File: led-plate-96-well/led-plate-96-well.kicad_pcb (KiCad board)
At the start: 2 copper layers, 175 x 100 mm, 2 parts, among them U1 TLC5947RHB, U2 A000053

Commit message: start main board
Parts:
- added C1: 100nF, Capacitor_SMD:C_0603_1608Metric, F.Cu at (100.2, 55.5)
- added C2: 10uF, Capacitor_SMD:C_0805_2012Metric, F.Cu at (92.2, 46.5)
- added D1: LED, SMD2835_WITH_STEP:LED_PLCC_2835, F.Cu at (99.1, 67.0)
- added D10: LED, SMD2835_WITH_STEP:LED_PLCC_2835, F.Cu at (112.4, 77.0)
- added D11: LED, SMD2835_WITH_STEP:LED_PLCC_2835, F.Cu at (112.4, 87.0)
- added D12: LED, SMD2835_WITH_STEP:LED_PLCC_2835, F.Cu at (112.4, 97.0)
- added D13: LED, SMD2835_WITH_STEP:LED_PLCC_2835, F.Cu at (112.4, 107.0)
- added D14: LED, SMD2835_WITH_STEP:LED_PLCC_2835, F.Cu at (112.4, 117.0)
- added D15: LED, SMD2835_WITH_STEP:LED_PLCC_2835, F.Cu at (112.4, 127.0)
- added D16: LED, SMD2835_WITH_STEP:LED_PLCC_2835, F.Cu at (112.4, 137.0)
- added D17: LED, SMD2835_WITH_STEP:LED_PLCC_2835, F.Cu at (124.1, 67.0)
- added D18: LED, SMD2835_WITH_STEP:LED_PLCC_2835, F.Cu at (124.1, 77.0)
- added D19: LED, SMD2835_WITH_STEP:LED_PLCC_2835, F.Cu at (124.1, 87.0)
- added D2: LED, SMD2835_WITH_STEP:LED_PLCC_2835, F.Cu at (99.1, 77.0)
- added D20: LED, SMD2835_WITH_STEP:LED_PLCC_2835, F.Cu at (124.1, 97.0)
- added D21: LED, SMD2835_WITH_STEP:LED_PLCC_2835, F.Cu at (124.1, 107.0)
- added D22: LED, SMD2835_WITH_STEP:LED_PLCC_2835, F.Cu at (124.1, 117.0)
- added D23: LED, SMD2835_WITH_STEP:LED_PLCC_2835, F.Cu at (124.1, 127.0)
- added D24: LED, SMD2835_WITH_STEP:LED_PLCC_2835, F.Cu at (124.1, 137.0)
- added D3: LED, SMD2835_WITH_STEP:LED_PLCC_2835, F.Cu at (99.1, 87.0)
- added D4: LED, SMD2835_WITH_STEP:LED_PLCC_2835, F.Cu at (99.1, 97.0)
- added D5: LED, SMD2835_WITH_STEP:LED_PLCC_2835, F.Cu at (99.1, 107.0)
- added D6: LED, SMD2835_WITH_STEP:LED_PLCC_2835, F.Cu at (99.1, 117.0)
- added D7: LED, SMD2835_WITH_STEP:LED_PLCC_2835, F.Cu at (99.1, 127.0)
- added D8: LED, SMD2835_WITH_STEP:LED_PLCC_2835, F.Cu at (99.1, 137.0)
- added D9: LED, SMD2835_WITH_STEP:LED_PLCC_2835, F.Cu at (112.4, 67.0)
- added J1: RAPC722X, RAPC722X:SWITCHCRAFT_RAPC722X, F.Cu at (52.0, 49.0)
- added R1: 2.49kΩ, Resistor_SMD:R_0402_1005Metric, F.Cu at (96.6, 55.6)
- added R2: 10kΩ, Resistor_SMD:R_0603_1608Metric, F.Cu at (92.0, 51.8)
- U1: value TLC5947RHB -> A000053; footprint Package_DFN_QFN:QFN-32-1EP_5x5mm_P0.5mm_EP3.45x3.45mm -> arduino_micro:A000053
- U2: value A000053 -> TLC5947RHB; footprint arduino_micro:A000053 -> Package_DFN_QFN:QFN-32-1EP_5x5mm_P0.5mm_EP3.45x3.45mm
- moved U1 59.3 mm to (57.4, 116.1)
- moved U2 46.6 mm to (105.4, 55.8), turned to 90 degrees
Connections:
- U1 pad 10: unconnected-(U1-OUT9-Pad10) -> Net-(U1-5(PWM))
- U1 pad 11: unconnected-(U1-OUT10-Pad11) -> Net-(U1-6(PWM)/A7)
- U1 pad 14: unconnected-(U1-OUT13-Pad14) -> Net-(U1-9(PWM)/A9)
- U1 pad 27: unconnected-(U1-IREF-Pad27) -> (no net)
- U1 pad 28: unconnected-(U1-VCC-Pad28) -> (no net)
- U1 pad 29: unconnected-(U1-GND-Pad29) -> +5V
- U1 pad 30: unconnected-(U1-BLANK-Pad30) -> Net-(U1-RESET-Pad30)
- U1 pad 31: unconnected-(U1-SCLK-Pad31) -> GND
- U1 pad 5: unconnected-(U1-OUT4-Pad5) -> Net-(U1-RESET-Pad30)
- U1 pad 6: unconnected-(U1-OUT5-Pad6) -> GND
- U1 pad 8: unconnected-(U1-OUT7-Pad8) -> Net-(U1-3(PWM)/SCL)
- U2 pad 1: unconnected-(U2-MOSI-Pad1) -> Net-(D1-K)
- U2 pad 10: unconnected-(U2-5(PWM)-Pad10) -> Net-(D10-K)
- U2 pad 11: unconnected-(U2-6(PWM)/A7-Pad11) -> Net-(D11-K)
- U2 pad 12: unconnected-(U2-7-Pad12) -> Net-(D12-K)
- U2 pad 13: unconnected-(U2-8/A8-Pad13) -> Net-(D13-K)
- U2 pad 14: unconnected-(U2-9(PWM)/A9-Pad14) -> Net-(D14-K)
- U2 pad 15: unconnected-(U2-10(PWM)/A10-Pad15) -> Net-(D15-K)
- U2 pad 16: unconnected-(U2-11(PWM)-Pad16) -> Net-(D16-K)
- U2 pad 17: unconnected-(U2-12/A11-Pad17) -> Net-(D17-K)
- U2 pad 18: unconnected-(U2-13(PWM)-Pad18) -> Net-(D18-K)
- U2 pad 19: unconnected-(U2-3.3V-Pad19) -> Net-(D19-K)
- U2 pad 2: unconnected-(U2-RX_LED/SS-Pad2) -> Net-(D2-K)
- U2 pad 20: unconnected-(U2-AREF-Pad20) -> Net-(D20-K)
- U2 pad 21: unconnected-(U2-A0-Pad21) -> Net-(D21-K)
- U2 pad 22: unconnected-(U2-A1-Pad22) -> Net-(D22-K)
- U2 pad 23: unconnected-(U2-A2-Pad23) -> Net-(D23-K)
- U2 pad 24: unconnected-(U2-A3-Pad24) -> Net-(D24-K)
- U2 pad 26: unconnected-(U2-A5-Pad26) -> Net-(U1-9(PWM)/A9)
- U2 pad 27: (no net) -> Net-(U2-IREF)
- U2 pad 28: (no net) -> +5V
- U2 pad 29: unconnected-(U2-+5V-Pad29) -> GND
- U2 pad 3: unconnected-(U2-1/TX-Pad3) -> Net-(D3-K)
- U2 pad 30: Net-(U2-RESET-Pad30) -> Net-(U1-6(PWM)/A7)
- U2 pad 31: Net-(U2-GND-Pad31) -> Net-(U1-5(PWM))
- U2 pad 32: unconnected-(U2-VIN-Pad32) -> Net-(U1-3(PWM)/SCL)
- U2 pad 33: unconnected-(U2-MISO-Pad33) -> GND
- U2 pad 4: unconnected-(U2-0/RX-Pad4) -> Net-(D4-K)
- U2 pad 5: Net-(U2-RESET-Pad30) -> Net-(D5-K)
- U2 pad 6: Net-(U2-GND-Pad31) -> Net-(D6-K)
- U2 pad 7: unconnected-(U2-2/SDA-Pad7) -> Net-(D7-K)
- U2 pad 8: unconnected-(U2-3(PWM)/SCL-Pad8) -> Net-(D8-K)
- U2 pad 9: unconnected-(U2-4/A6-Pad9) -> Net-(D9-K)
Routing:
- net Net-(U1-9(PWM)/A9): track 0.00 -> 110.7 mm
- net Net-(D24-K): track 0.00 -> 107.3 mm
- net Net-(U1-6(PWM)/A7): track 0.00 -> 101.6 mm
- net Net-(U1-5(PWM)): track 0.00 -> 98.2 mm
- net Net-(D23-K): track 0.00 -> 95.3 mm
- net Net-(U1-3(PWM)/SCL): track 0.00 -> 92.2 mm
- net Net-(D16-K): track 0.00 -> 88.9 mm
- net Net-(D22-K): track 0.00 -> 83.8 mm
- net Net-(D8-K): track 0.00 -> 81.8 mm
- net Net-(D15-K): track 0.00 -> 78.0 mm
- net Net-(D21-K): track 0.00 -> 72.3 mm
- net Net-(D7-K): track 0.00 -> 71.6 mm
- net Net-(D14-K): track 0.00 -> 67.1 mm
- net Net-(D6-K): track 0.00 -> 61.4 mm
- net Net-(D20-K): track 0.00 -> 60.7 mm
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- added copper zone on In2.Cu, net +5V
- added copper zone on In1.Cu, net GND
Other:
- copper layers 2 -> 4

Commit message: layout leds
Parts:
- added C10: 10uF, Capacitor_SMD:C_0805_2012Metric, F.Cu at (50.6, 69.5)
- added C11: 10uF, Capacitor_SMD:C_0805_2012Metric, F.Cu at (50.6, 72.5)
- added C12: 100nF, Capacitor_SMD:C_0603_1608Metric, F.Cu at (59.9, 64.0)
- added C13: 10uF, Capacitor_SMD:C_0805_2012Metric, F.Cu at (50.6, 75.5)
- added C3: 100uF, Capacitor_SMD:C_1206_3216Metric, F.Cu at (64.7, 64.9)
- added C4: 10uF, Capacitor_SMD:C_0805_2012Metric, F.Cu at (50.6, 57.5)
- added C5: 10uF, Capacitor_SMD:C_0805_2012Metric, F.Cu at (50.6, 60.5)
- added C6: 100nF, Capacitor_SMD:C_0603_1608Metric, F.Cu at (59.9, 59.0)
- added C7: 10uF, Capacitor_SMD:C_0805_2012Metric, F.Cu at (50.6, 63.5)
- added C8: 10uF, Capacitor_SMD:C_0805_2012Metric, F.Cu at (50.6, 66.5)
- added C9: 100nF, Capacitor_SMD:C_0603_1608Metric, F.Cu at (59.9, 61.5)
- added D25: LED, SMD2835_WITH_STEP:LED_PLCC_2835, F.Cu at (112.7, 58.5)
- added D26: LED, SMD2835_WITH_STEP:LED_PLCC_2835, F.Cu at (112.7, 67.5)
- added D27: LED, SMD2835_WITH_STEP:LED_PLCC_2835, F.Cu at (112.7, 76.5)
- added D28: LED, SMD2835_WITH_STEP:LED_PLCC_2835, F.Cu at (112.7, 85.5)
- added D29: LED, SMD2835_WITH_STEP:LED_PLCC_2835, F.Cu at (112.7, 94.5)
- added D30: LED, SMD2835_WITH_STEP:LED_PLCC_2835, F.Cu at (112.7, 103.5)
- added D31: LED, SMD2835_WITH_STEP:LED_PLCC_2835, F.Cu at (112.7, 112.5)
- added D32: LED, SMD2835_WITH_STEP:LED_PLCC_2835, F.Cu at (112.7, 121.5)
- added D33: LED, SMD2835_WITH_STEP:LED_PLCC_2835, F.Cu at (121.7, 58.5)
- added D34: LED, SMD2835_WITH_STEP:LED_PLCC_2835, F.Cu at (121.7, 67.5)
- added D35: LED, SMD2835_WITH_STEP:LED_PLCC_2835, F.Cu at (121.7, 76.5)
- added D36: LED, SMD2835_WITH_STEP:LED_PLCC_2835, F.Cu at (121.7, 85.5)
- added D37: LED, SMD2835_WITH_STEP:LED_PLCC_2835, F.Cu at (121.7, 94.5)
- added D38: LED, SMD2835_WITH_STEP:LED_PLCC_2835, F.Cu at (121.7, 103.5)
- added D39: LED, SMD2835_WITH_STEP:LED_PLCC_2835, F.Cu at (121.7, 112.5)
- added D40: LED, SMD2835_WITH_STEP:LED_PLCC_2835, F.Cu at (121.7, 121.5)
- added D41: LED, SMD2835_WITH_STEP:LED_PLCC_2835, F.Cu at (130.7, 58.5)
- added D42: LED, SMD2835_WITH_STEP:LED_PLCC_2835, F.Cu at (130.7, 67.5)
- added D43: LED, SMD2835_WITH_STEP:LED_PLCC_2835, F.Cu at (130.7, 76.5)
- added D44: LED, SMD2835_WITH_STEP:LED_PLCC_2835, F.Cu at (130.7, 85.5)
- added D45: LED, SMD2835_WITH_STEP:LED_PLCC_2835, F.Cu at (130.7, 94.5)
- added D46: LED, SMD2835_WITH_STEP:LED_PLCC_2835, F.Cu at (130.7, 103.5)
- added D47: LED, SMD2835_WITH_STEP:LED_PLCC_2835, F.Cu at (130.7, 112.5)
- added D48: LED, SMD2835_WITH_STEP:LED_PLCC_2835, F.Cu at (130.7, 121.5)
- added D49: LED, SMD2835_WITH_STEP:LED_PLCC_2835, F.Cu at (139.7, 58.5)
- added D50: LED, SMD2835_WITH_STEP:LED_PLCC_2835, F.Cu at (139.7, 67.5)
- added D51: LED, SMD2835_WITH_STEP:LED_PLCC_2835, F.Cu at (139.7, 76.5)
- added D52: LED, SMD2835_WITH_STEP:LED_PLCC_2835, F.Cu at (139.7, 85.5)
- added D53: LED, SMD2835_WITH_STEP:LED_PLCC_2835, F.Cu at (139.7, 94.5)
- added D54: LED, SMD2835_WITH_STEP:LED_PLCC_2835, F.Cu at (139.7, 103.5)
- added D55: LED, SMD2835_WITH_STEP:LED_PLCC_2835, F.Cu at (139.7, 112.5)
- added D56: LED, SMD2835_WITH_STEP:LED_PLCC_2835, F.Cu at (139.7, 121.5)
- added D57: LED, SMD2835_WITH_STEP:LED_PLCC_2835, F.Cu at (148.7, 58.5)
- added D58: LED, SMD2835_WITH_STEP:LED_PLCC_2835, F.Cu at (148.7, 67.5)
- added D59: LED, SMD2835_WITH_STEP:LED_PLCC_2835, F.Cu at (148.7, 76.5)
- added D60: LED, SMD2835_WITH_STEP:LED_PLCC_2835, F.Cu at (148.7, 85.5)
- added D61: LED, SMD2835_WITH_STEP:LED_PLCC_2835, F.Cu at (148.7, 94.5)
- added D62: LED, SMD2835_WITH_STEP:LED_PLCC_2835, F.Cu at (148.7, 103.5)
- added D63: LED, SMD2835_WITH_STEP:LED_PLCC_2835, F.Cu at (148.7, 112.5)
- added D64: LED, SMD2835_WITH_STEP:LED_PLCC_2835, F.Cu at (148.7, 121.5)
- added D65: LED, SMD2835_WITH_STEP:LED_PLCC_2835, F.Cu at (157.7, 58.5)
- added D66: LED, SMD2835_WITH_STEP:LED_PLCC_2835, F.Cu at (157.7, 67.5)
- added D67: LED, SMD2835_WITH_STEP:LED_PLCC_2835, F.Cu at (157.7, 76.5)
- added D68: LED, SMD2835_WITH_STEP:LED_PLCC_2835, F.Cu at (157.7, 85.5)
- added D69: LED, SMD2835_WITH_STEP:LED_PLCC_2835, F.Cu at (157.7, 94.5)
- added D70: LED, SMD2835_WITH_STEP:LED_PLCC_2835, F.Cu at (157.7, 103.5)
- added D71: LED, SMD2835_WITH_STEP:LED_PLCC_2835, F.Cu at (157.7, 112.5)
- added D72: LED, SMD2835_WITH_STEP:LED_PLCC_2835, F.Cu at (157.7, 121.5)
- added D73: LED, SMD2835_WITH_STEP:LED_PLCC_2835, F.Cu at (166.7, 58.5)
- added D74: LED, SMD2835_WITH_STEP:LED_PLCC_2835, F.Cu at (166.7, 67.5)
- added D75: LED, SMD2835_WITH_STEP:LED_PLCC_2835, F.Cu at (166.7, 76.5)
- added D76: LED, SMD2835_WITH_STEP:LED_PLCC_2835, F.Cu at (166.7, 85.5)
- added D77: LED, SMD2835_WITH_STEP:LED_PLCC_2835, F.Cu at (166.7, 94.5)
- added D78: LED, SMD2835_WITH_STEP:LED_PLCC_2835, F.Cu at (166.7, 103.5)
- added D79: LED, SMD2835_WITH_STEP:LED_PLCC_2835, F.Cu at (166.7, 112.5)
- added D80: LED, SMD2835_WITH_STEP:LED_PLCC_2835, F.Cu at (166.7, 121.5)
- added D81: LED, SMD2835_WITH_STEP:LED_PLCC_2835, F.Cu at (175.7, 58.5)
- added D82: LED, SMD2835_WITH_STEP:LED_PLCC_2835, F.Cu at (175.7, 67.5)
- added D83: LED, SMD2835_WITH_STEP:LED_PLCC_2835, F.Cu at (175.7, 76.5)
- added D84: LED, SMD2835_WITH_STEP:LED_PLCC_2835, F.Cu at (175.7, 85.5)
- added D85: LED, SMD2835_WITH_STEP:LED_PLCC_2835, F.Cu at (175.7, 94.5)
- added D86: LED, SMD2835_WITH_STEP:LED_PLCC_2835, F.Cu at (175.7, 103.5)
- added D87: LED, SMD2835_WITH_STEP:LED_PLCC_2835, F.Cu at (175.7, 112.5)
- added D88: LED, SMD2835_WITH_STEP:LED_PLCC_2835, F.Cu at (175.7, 121.5)
- added D89: LED, SMD2835_WITH_STEP:LED_PLCC_2835, F.Cu at (184.7, 58.5)
- added D90: LED, SMD2835_WITH_STEP:LED_PLCC_2835, F.Cu at (184.7, 67.5)
- added D91: LED, SMD2835_WITH_STEP:LED_PLCC_2835, F.Cu at (184.7, 76.5)
- added D92: LED, SMD2835_WITH_STEP:LED_PLCC_2835, F.Cu at (184.7, 85.5)
- added D93: LED, SMD2835_WITH_STEP:LED_PLCC_2835, F.Cu at (184.7, 94.5)
- added D94: LED, SMD2835_WITH_STEP:LED_PLCC_2835, F.Cu at (184.7, 103.5)
- added D95: LED, SMD2835_WITH_STEP:LED_PLCC_2835, F.Cu at (184.7, 112.5)
- added D96: LED, SMD2835_WITH_STEP:LED_PLCC_2835, F.Cu at (184.7, 121.5)
- added R4: 2.49kΩ, Resistor_SMD:R_0402_1005Metric, F.Cu at (63.3, 58.2)
- added R6: 2.49kΩ, Resistor_SMD:R_0402_1005Metric, F.Cu at (63.3, 60.2)
- added R8: 2.49kΩ, Resistor_SMD:R_0402_1005Metric, F.Cu at (63.3, 62.2)
- added REF**: plate_adapater_96_well, plate_adapater_96_well:plate_adapater_96_well, F.Cu at (135.4, 90.0)
- added U3: TLC5947RHB, Package_DFN_QFN:QFN-32-1EP_5x5mm_P0.5mm_EP3.45x3.45mm, F.Cu at (121.7, 40.5)
- added U4: TLC5947RHB, Package_DFN_QFN:QFN-32-1EP_5x5mm_P0.5mm_EP3.45x3.45mm, F.Cu at (148.7, 40.5)
- added U5: TLC5947RHB, Package_DFN_QFN:QFN-32-1EP_5x5mm_P0.5mm_EP3.45x3.45mm, F.Cu at (175.7, 40.5)
- moved C2 42.4 mm to (50.6, 54.5)
- moved C1 40.3 mm to (59.9, 56.5)
- moved R2 35.4 mm to (59.9, 66.5)
- moved R1 33.3 mm to (63.3, 56.2)
- moved D24 25.6 mm to (103.7, 121.5), turned to 0 degrees
- moved D23 25.1 mm to (103.7, 112.5), turned to 0 degrees
- moved D22 24.5 mm to (103.7, 103.5), turned to 0 degrees
- moved D21 24.0 mm to (103.7, 94.5), turned to 0 degrees
- moved D16 23.5 mm to (94.7, 121.5), turned to 0 degrees
- moved D20 23.5 mm to (103.7, 85.5), turned to 0 degrees
- moved D19 23.0 mm to (103.7, 76.5), turned to 0 degrees
- moved D15 22.9 mm to (94.7, 112.5), turned to 0 degrees
- moved D18 22.5 mm to (103.7, 67.5), turned to 0 degrees
- moved D14 22.3 mm to (94.7, 103.5), turned to 0 degrees
- moved D17 22.1 mm to (103.7, 58.5), turned to 0 degrees
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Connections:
- U1 pad 30: Net-(U1-RESET-Pad30) -> unconnected-(U1-RESET-Pad30)_1
- U1 pad 5: Net-(U1-RESET-Pad30) -> unconnected-(U1-RESET-Pad30)
- U2 pad 25: unconnected-(U2-SOUT-Pad25) -> Net-(U2-SOUT)
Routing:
- net Net-(U1-9(PWM)/A9): track 110.7 -> 0.00 mm
- net Net-(D24-K): track 107.3 -> 0.00 mm
- net Net-(U1-6(PWM)/A7): track 101.6 -> 0.00 mm
- net Net-(U1-5(PWM)): track 98.2 -> 0.00 mm
- net Net-(D23-K): track 95.3 -> 0.00 mm
- net Net-(U1-3(PWM)/SCL): track 92.2 -> 0.00 mm
- net Net-(D16-K): track 88.9 -> 0.00 mm
- net Net-(D22-K): track 83.8 -> 0.00 mm
- net Net-(D8-K): track 81.8 -> 0.00 mm
- net Net-(D15-K): track 78.0 -> 0.00 mm
- net Net-(D21-K): track 72.3 -> 0.00 mm
- net Net-(D7-K): track 71.6 -> 0.00 mm
- net Net-(D14-K): track 67.1 -> 0.00 mm
- net Net-(D6-K): track 61.4 -> 0.00 mm
- net Net-(D20-K): track 60.7 -> 0.00 mm
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- removed copper zone on In2.Cu, net +5V
- removed copper zone on In1.Cu, net GND
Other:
- board size 175 x 100 mm -> 165.8 x 112.7 mm

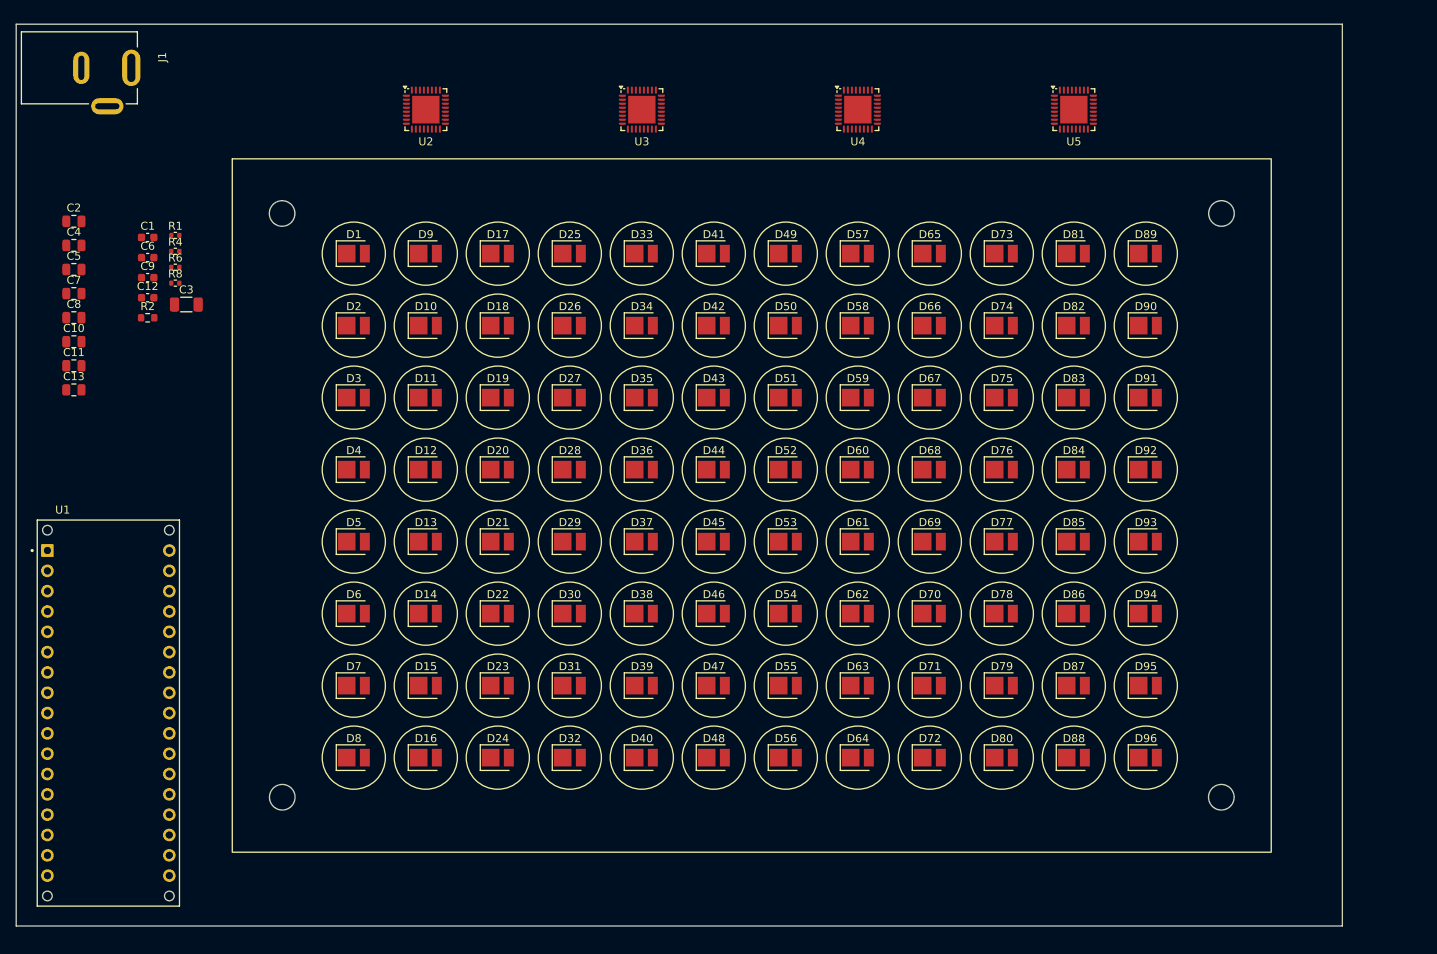
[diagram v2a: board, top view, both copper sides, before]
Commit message: basic layout for all components
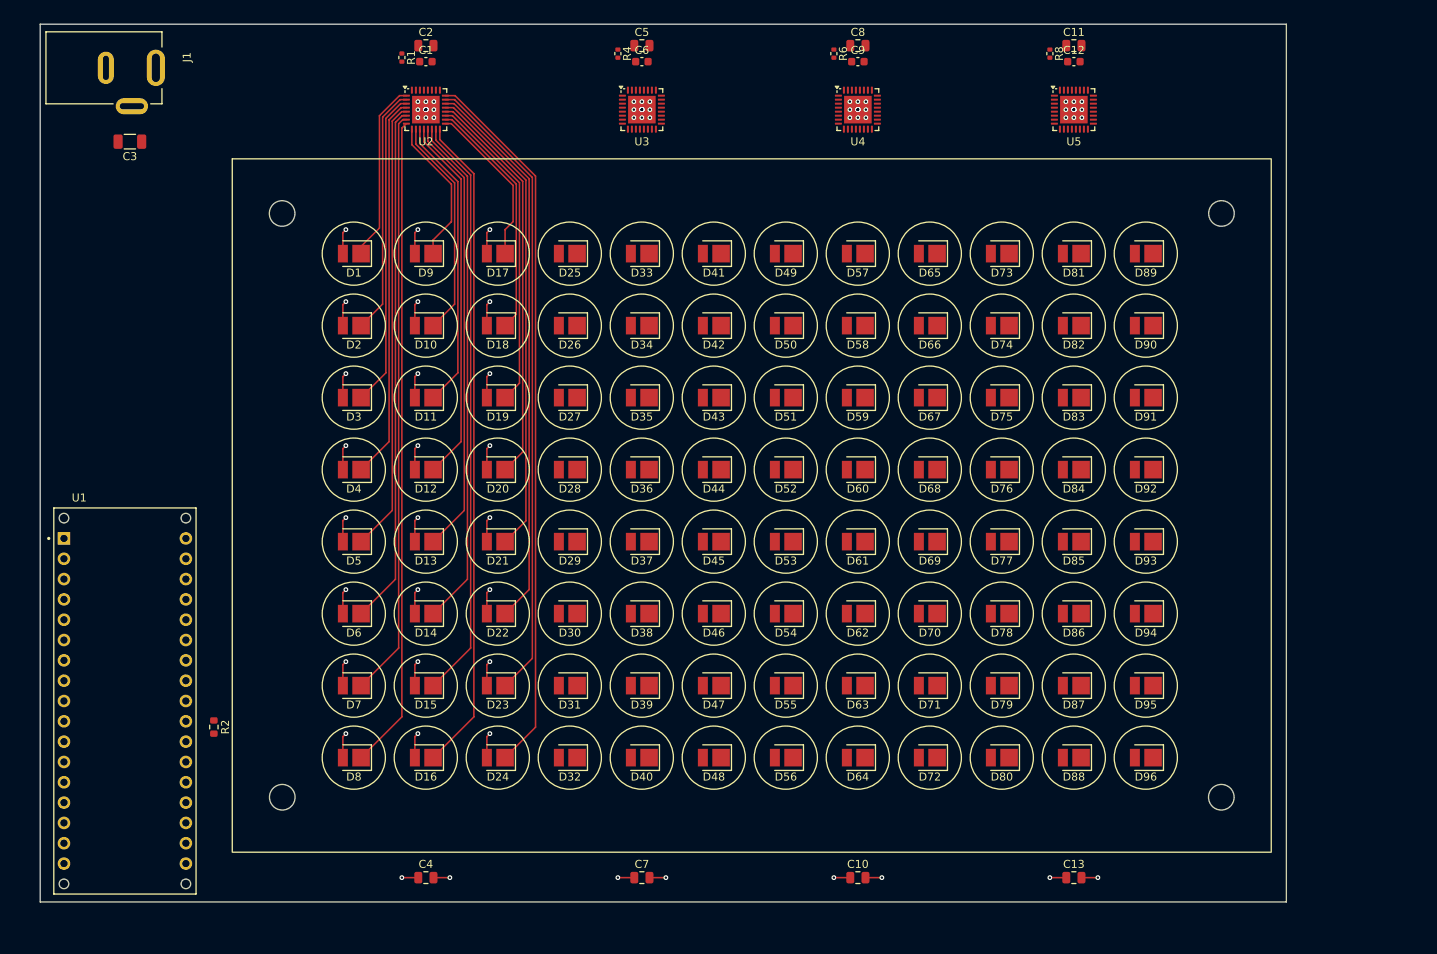
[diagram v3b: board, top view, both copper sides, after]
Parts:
- moved C13 139.1 mm to (175.7, 136.5)
- moved C11 131.3 mm to (175.7, 32.5)
- moved C12 119.5 mm to (175.7, 34.5)
- moved C10 118.7 mm to (148.7, 136.5)
- moved R8 113.0 mm to (172.7, 33.5), turned to -90 degrees
- moved C8 103.7 mm to (148.7, 32.5)
- moved C7 101.8 mm to (121.7, 136.5)
- moved C9 92.8 mm to (148.7, 34.5)
- moved C4 90.5 mm to (94.7, 136.5)
- moved R6 86.5 mm to (145.7, 33.5), turned to -90 degrees
- moved C5 76.3 mm to (121.7, 32.5)
- moved C6 66.5 mm to (121.7, 34.5)
- moved R4 60.6 mm to (118.7, 33.5), turned to -90 degrees
- moved R2 51.8 mm to (68.2, 117.7), turned to -90 degrees
- moved C2 49.2 mm to (94.7, 32.5)
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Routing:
- net Net-(D24-K): track 0.00 -> 89.7 mm
- net +5V: track 0.00 -> 83.9 mm, vias 0 -> 28
- net Net-(D16-K): track 0.00 -> 82.4 mm
- net Net-(D8-K): track 0.00 -> 81.6 mm
- net Net-(D23-K): track 0.00 -> 79.8 mm
- net Net-(D7-K): track 0.00 -> 73.4 mm
- net Net-(D15-K): track 0.00 -> 73.3 mm
- net Net-(D22-K): track 0.00 -> 70.0 mm
- net Net-(D6-K): track 0.00 -> 64.9 mm
- net Net-(D14-K): track 0.00 -> 64.2 mm
- net Net-(D21-K): track 0.00 -> 60.1 mm
- net Net-(D5-K): track 0.00 -> 56.4 mm
- net GND: track 0.00 -> 56.2 mm, vias 0 -> 76
- net Net-(D13-K): track 0.00 -> 55.1 mm
- net Net-(D20-K): track 0.00 -> 50.2 mm
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- added copper zone on In2.Cu, net +5V
- added copper zone on In1.Cu, net GND
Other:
- board size 165.8 x 112.7 mm -> 155.8 x 109.7 mm

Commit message: finished routing traces
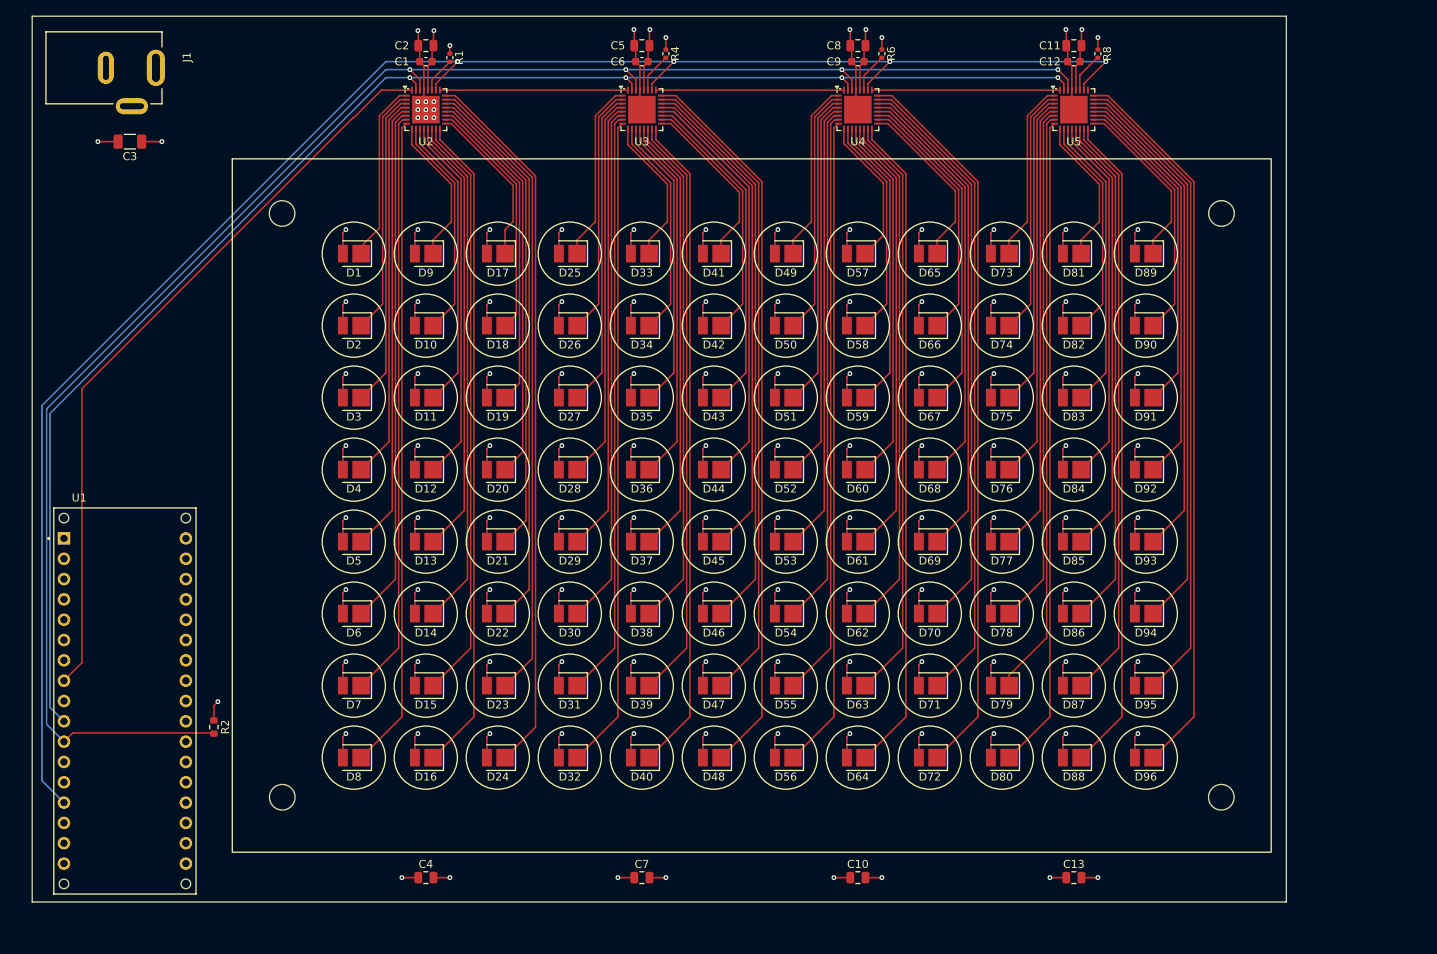
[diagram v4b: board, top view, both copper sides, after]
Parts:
- moved R1 6.00 mm to (97.7, 34.0)
- moved R4 6.00 mm to (124.7, 33.5)
- moved R6 6.00 mm to (151.7, 33.5)
- moved R8 6.00 mm to (178.7, 33.5)
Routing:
- net +5V: track 83.9 -> 347.6 mm, vias 28 -> 106
- net Net-(U1-9(PWM)/A9): track 0.00 -> 220.4 mm, vias 0 -> 4
- net Net-(U1-6(PWM)/A7): track 0.00 -> 218.0 mm, vias 0 -> 4
- net Net-(U1-5(PWM)): track 0.00 -> 190.1 mm, vias 0 -> 4
- net Net-(U1-3(PWM)/SCL): track 0.00 -> 94.1 mm
- net Net-(D96-K): track 0.00 -> 91.1 mm
- net Net-(D72-K): track 0.00 -> 91.1 mm
- net Net-(D48-K): track 0.00 -> 91.1 mm
- net Net-(D40-K): track 0.00 -> 82.4 mm
- net Net-(D88-K): track 0.00 -> 82.4 mm
- net Net-(D64-K): track 0.00 -> 82.4 mm
- net Net-(D32-K): track 0.00 -> 81.6 mm
- net Net-(D80-K): track 0.00 -> 81.6 mm
- net Net-(D56-K): track 0.00 -> 81.6 mm
- net Net-(D95-K): track 0.00 -> 81.3 mm
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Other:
- board size 155.8 x 109.7 mm -> 156.8 x 110.7 mm
